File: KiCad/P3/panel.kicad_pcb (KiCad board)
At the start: 2 copper layers, 94 x 95.5 mm, 359 parts, among them J1 USB_C_Receptacle_USB2.0, J2 SM04B-SRSS-TB(LF)(SN), U1 USBLC6-2SC6

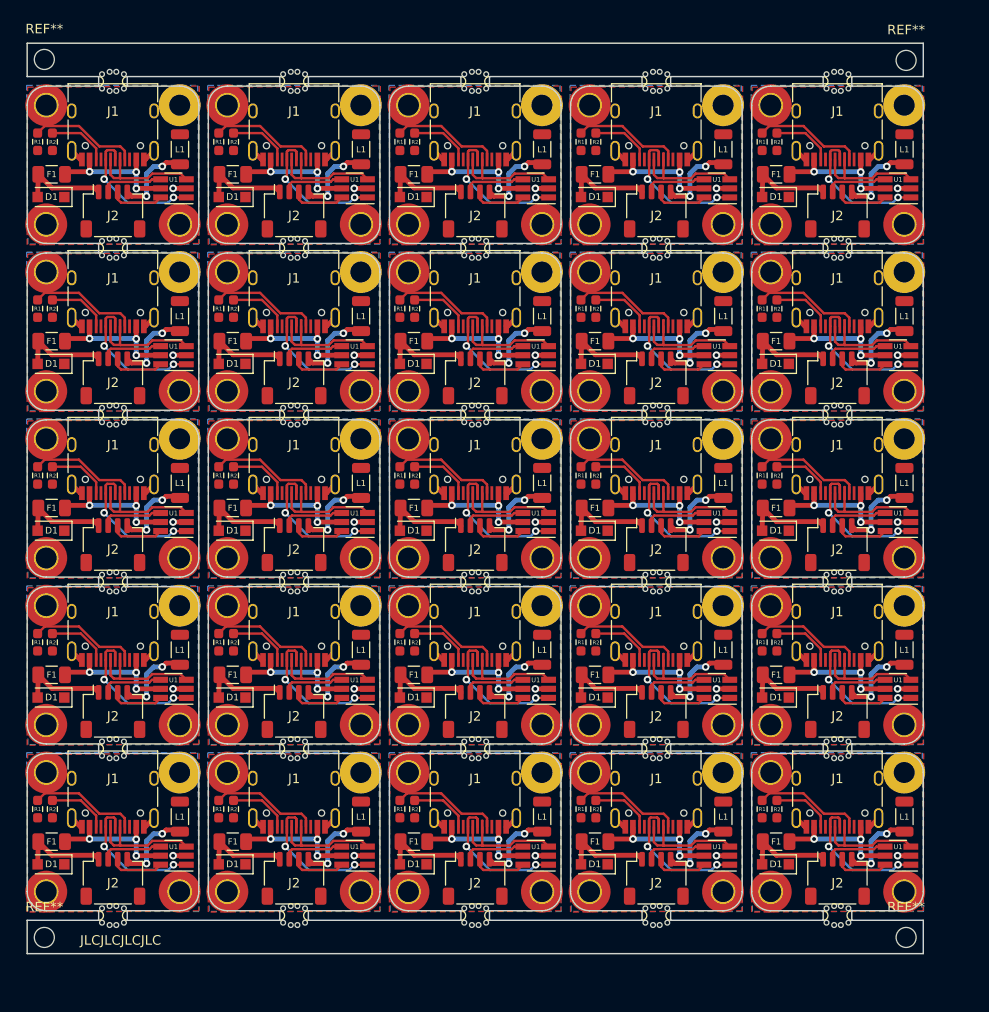
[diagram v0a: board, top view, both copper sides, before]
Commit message: Update P3 panel to improve mousebites and allow soldering before splitting
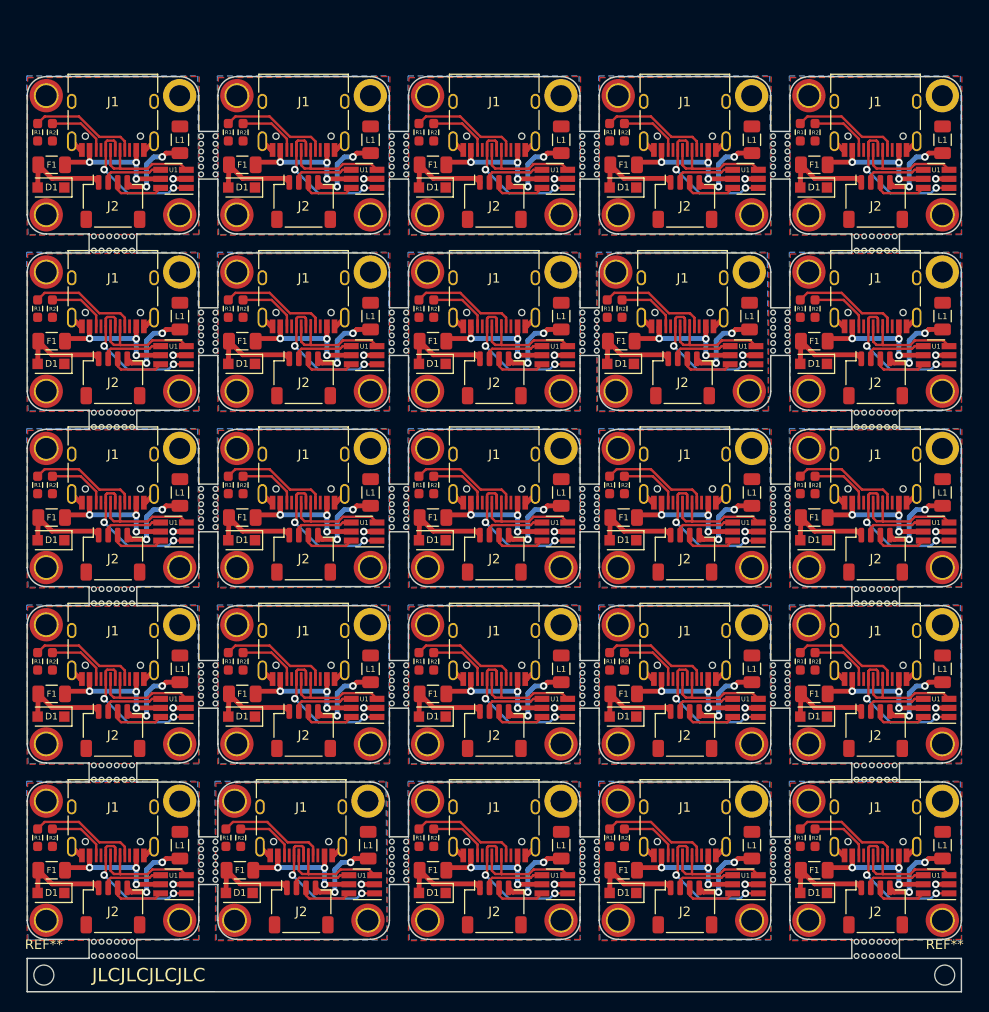
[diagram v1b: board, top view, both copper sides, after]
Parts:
- removed the D1 at (93.5, 101.0)
- removed the D1 at (17.5, 83.5)
- removed the D1 at (93.5, 66.0)
- removed the D1 at (74.5, 66.0)
- removed the D1 at (55.5, 66.0)
- removed the D1 at (36.5, 66.0)
- removed the D1 at (17.5, 66.0)
- removed the D1 at (93.5, 48.5)
- removed the D1 at (74.5, 48.5)
- removed the D1 at (55.5, 48.5)
- removed the D1 at (36.5, 48.5)
- removed the D1 at (74.5, 101.0)
- removed the D1 at (17.5, 48.5)
- removed the D1 at (93.5, 31.0)
- removed the D1 at (74.5, 31.0)
- removed the D1 at (55.5, 31.0)
- removed the D1 at (36.5, 31.0)
- removed the D1 at (17.5, 31.0)
- removed the D1 at (55.5, 101.0)
- removed the D1 at (36.5, 101.0)
- removed the D1 at (17.5, 101.0)
- removed the D1 at (93.5, 83.5)
- removed the D1 at (74.5, 83.5)
- removed the D1 at (55.5, 83.5)
- removed the D1 at (36.5, 83.5)
- removed the F1 at (74.6, 98.6)
- removed the F1 at (55.6, 81.1)
- removed the F1 at (74.6, 63.6)
- removed the F1 at (93.6, 63.6)
- removed the F1 at (17.6, 63.6)
- removed the F1 at (36.6, 63.6)
- removed the F1 at (55.6, 63.6)
- removed the F1 at (74.6, 46.1)
- removed the F1 at (93.6, 46.1)
- removed the F1 at (17.6, 46.1)
- removed the F1 at (36.6, 46.1)
- removed the F1 at (93.6, 98.6)
- removed the F1 at (55.6, 46.1)
- removed the F1 at (93.6, 28.6)
- removed the F1 at (74.6, 28.6)
- removed the F1 at (55.6, 28.6)
- removed the F1 at (36.6, 28.6)
- removed the F1 at (17.6, 28.6)
- removed the F1 at (17.6, 98.6)
- removed the F1 at (36.6, 98.6)
- removed the F1 at (55.6, 98.6)
- removed the F1 at (74.6, 81.1)
- removed the F1 at (93.6, 81.1)
- removed the F1 at (17.6, 81.1)
- removed the F1 at (36.6, 81.1)
- removed the G1 at (81.0, 99.8)
- removed the G1 at (62.0, 82.3)
- removed the G1 at (81.0, 64.8)
- removed the G1 at (100.0, 64.8)
- removed the G1 at (24.0, 64.8)
- removed the G1 at (43.0, 64.8)
- removed the G1 at (62.0, 64.8)
- removed the G1 at (81.0, 47.3)
- removed the G1 at (100.0, 47.3)
- removed the G1 at (24.0, 47.3)
- removed the G1 at (43.0, 47.3)
- removed the G1 at (100.0, 99.8)
- removed the G1 at (62.0, 47.3)
- removed the G1 at (100.0, 29.8)
- removed the G1 at (81.0, 29.8)
- removed the G1 at (62.0, 29.8)
- removed the G1 at (43.0, 29.8)
- removed the G1 at (24.0, 29.8)
- removed the G1 at (24.0, 99.8)
- removed the G1 at (43.0, 99.8)
- removed the G1 at (62.0, 99.8)
- removed the G1 at (81.0, 82.3)
- removed the G1 at (100.0, 82.3)
- removed the G1 at (24.0, 82.3)
- removed the G1 at (43.0, 82.3)
- removed the J1 at (100.0, 93.0)
- removed the J1 at (43.0, 75.5)
- removed the J1 at (100.0, 58.0)
- removed the J1 at (81.0, 58.0)
- removed the J1 at (62.0, 58.0)
- removed the J1 at (24.0, 58.0)
- removed the J1 at (43.0, 58.0)
- removed the J1 at (100.0, 40.5)
- removed the J1 at (81.0, 40.5)
- removed the J1 at (62.0, 40.5)
- removed the J1 at (24.0, 40.5)
- removed the J1 at (81.0, 93.0)
- removed the J1 at (43.0, 40.5)
- removed the J1 at (100.0, 23.0)
- removed the J1 at (81.0, 23.0)
- removed the J1 at (62.0, 23.0)
- removed the J1 at (43.0, 23.0)
- removed the J1 at (24.0, 23.0)
- removed the J1 at (62.0, 93.0)
- removed the J1 at (24.0, 93.0)
- removed the J1 at (43.0, 93.0)
- removed the J1 at (100.0, 75.5)
- removed the J1 at (81.0, 75.5)
- removed the J1 at (62.0, 75.5)
- removed the J1 at (24.0, 75.5)
- removed the J2 at (100.0, 102.4)
- removed the J2 at (62.0, 84.9)
- removed the J2 at (100.0, 67.4)
- removed the J2 at (81.0, 67.4)
- removed the J2 at (43.0, 67.4)
- removed the J2 at (24.0, 67.4)
- removed the J2 at (62.0, 67.4)
- removed the J2 at (100.0, 49.9)
- removed the J2 at (81.0, 49.9)
- removed the J2 at (43.0, 49.9)
- removed the J2 at (24.0, 49.9)
- removed the J2 at (81.0, 102.4)
- removed the J2 at (62.0, 49.9)
- removed the J2 at (100.0, 32.4)
- removed the J2 at (81.0, 32.4)
- removed the J2 at (62.0, 32.4)
- removed the J2 at (43.0, 32.4)
- removed the J2 at (24.0, 32.4)
- removed the J2 at (43.0, 102.4)
- removed the J2 at (24.0, 102.4)
- removed the J2 at (62.0, 102.4)
- removed the J2 at (100.0, 84.9)
- removed the J2 at (81.0, 84.9)
- removed the J2 at (43.0, 84.9)
- removed the J2 at (24.0, 84.9)
- removed the L1 at (107.0, 96.0)
- removed the L1 at (50.0, 78.5)
- removed the L1 at (107.0, 61.0)
- removed the L1 at (88.0, 61.0)
- removed the L1 at (31.0, 61.0)
- removed the L1 at (69.0, 61.0)
- removed the L1 at (50.0, 61.0)
- removed the L1 at (107.0, 43.5)
- removed the L1 at (88.0, 43.5)
- removed the L1 at (31.0, 43.5)
- removed the L1 at (69.0, 43.5)
- removed the L1 at (88.0, 96.0)
- removed the L1 at (50.0, 43.5)
- removed the L1 at (107.0, 26.0)
- removed the L1 at (88.0, 26.0)
- removed the L1 at (69.0, 26.0)
- removed the L1 at (50.0, 26.0)
- removed the L1 at (31.0, 26.0)
- removed the L1 at (31.0, 96.0)
- removed the L1 at (69.0, 96.0)
- removed the L1 at (50.0, 96.0)
- removed the L1 at (107.0, 78.5)
- removed the L1 at (88.0, 78.5)
- removed the L1 at (31.0, 78.5)
- removed the L1 at (69.0, 78.5)
- removed the MH1 at (93.0, 91.3)
- removed the MH1 at (55.0, 73.8)
- removed the MH1 at (93.0, 56.3)
- removed the MH1 at (74.0, 56.3)
- removed the MH1 at (36.0, 56.3)
- removed the MH1 at (17.0, 56.3)
- removed the MH1 at (55.0, 56.3)
- removed the MH1 at (93.0, 38.8)
- removed the MH1 at (74.0, 38.8)
- removed the MH1 at (36.0, 38.8)
- removed the MH1 at (17.0, 38.8)
- removed the MH1 at (74.0, 91.3)
- removed the MH1 at (55.0, 38.8)
- removed the MH1 at (93.0, 21.3)
- removed the MH1 at (74.0, 21.3)
- removed the MH1 at (55.0, 21.3)
- removed the MH1 at (36.0, 21.3)
- removed the MH1 at (17.0, 21.3)
- removed the MH1 at (36.0, 91.3)
- removed the MH1 at (17.0, 91.3)
- removed the MH1 at (55.0, 91.3)
- removed the MH1 at (93.0, 73.8)
- removed the MH1 at (74.0, 73.8)
- removed the MH1 at (36.0, 73.8)
- removed the MH1 at (17.0, 73.8)
- removed the MH2 at (107.0, 91.3)
- removed the MH2 at (69.0, 73.8)
- removed the MH2 at (107.0, 56.3)
- removed the MH2 at (88.0, 56.3)
- removed the MH2 at (50.0, 56.3)
- removed the MH2 at (31.0, 56.3)
- removed the MH2 at (69.0, 56.3)
- removed the MH2 at (107.0, 38.8)
- removed the MH2 at (88.0, 38.8)
- removed the MH2 at (50.0, 38.8)
- removed the MH2 at (31.0, 38.8)
- removed the MH2 at (88.0, 91.3)
- removed the MH2 at (69.0, 38.8)
- removed the MH2 at (107.0, 21.3)
- removed the MH2 at (88.0, 21.3)
- removed the MH2 at (69.0, 21.3)
- removed the MH2 at (50.0, 21.3)
- removed the MH2 at (31.0, 21.3)
- removed the MH2 at (50.0, 91.3)
- removed the MH2 at (31.0, 91.3)
- removed the MH2 at (69.0, 91.3)
- removed the MH2 at (107.0, 73.8)
- removed the MH2 at (88.0, 73.8)
- removed the MH2 at (50.0, 73.8)
- removed the MH2 at (31.0, 73.8)
- removed the MH3 at (93.0, 103.8)
- removed the MH3 at (55.0, 86.3)
- removed the MH3 at (93.0, 68.8)
- removed the MH3 at (74.0, 68.8)
- removed the MH3 at (36.0, 68.8)
- removed the MH3 at (17.0, 68.8)
- removed the MH3 at (55.0, 68.8)
- removed the MH3 at (93.0, 51.3)
- removed the MH3 at (74.0, 51.3)
- removed the MH3 at (36.0, 51.3)
- removed the MH3 at (17.0, 51.3)
- removed the MH3 at (74.0, 103.8)
- removed the MH3 at (55.0, 51.3)
- removed the MH3 at (93.0, 33.8)
- removed the MH3 at (74.0, 33.8)
- removed the MH3 at (55.0, 33.8)
- removed the MH3 at (36.0, 33.8)
- removed the MH3 at (17.0, 33.8)
- removed the MH3 at (36.0, 103.8)
- removed the MH3 at (17.0, 103.8)
- removed the MH3 at (55.0, 103.8)
- removed the MH3 at (93.0, 86.3)
- removed the MH3 at (74.0, 86.3)
- removed the MH3 at (36.0, 86.3)
- removed the MH3 at (17.0, 86.3)
- removed the MH4 at (107.0, 103.8)
- removed the MH4 at (69.0, 86.3)
- removed the MH4 at (107.0, 68.8)
- removed the MH4 at (88.0, 68.8)
- removed the MH4 at (50.0, 68.8)
- removed the MH4 at (31.0, 68.8)
- removed the MH4 at (69.0, 68.8)
- removed the MH4 at (107.0, 51.3)
- removed the MH4 at (88.0, 51.3)
- removed the MH4 at (50.0, 51.3)
- removed the MH4 at (31.0, 51.3)
- removed the MH4 at (88.0, 103.8)
- removed the MH4 at (69.0, 51.3)
- removed the MH4 at (107.0, 33.8)
- removed the MH4 at (88.0, 33.8)
- removed the MH4 at (69.0, 33.8)
- removed the MH4 at (50.0, 33.8)
- removed the MH4 at (31.0, 33.8)
- removed the MH4 at (50.0, 103.8)
- removed the MH4 at (31.0, 103.8)
- removed the MH4 at (69.0, 103.8)
- removed the MH4 at (107.0, 86.3)
- removed the MH4 at (88.0, 86.3)
- removed the MH4 at (50.0, 86.3)
- removed the MH4 at (31.0, 86.3)
- removed the R1 at (92.1, 95.2)
- removed the R1 at (35.1, 77.7)
- removed the R1 at (92.1, 60.2)
- removed the R1 at (73.1, 60.2)
- removed the R1 at (54.1, 60.2)
- removed the R1 at (16.1, 60.2)
- removed the R1 at (35.1, 60.2)
- removed the R1 at (92.1, 42.7)
- removed the R1 at (73.1, 42.7)
- removed the R1 at (54.1, 42.7)
- removed the R1 at (16.1, 42.7)
- removed the R1 at (73.1, 95.2)
- removed the R1 at (35.1, 42.7)
- removed the R1 at (92.1, 25.2)
- removed the R1 at (73.1, 25.2)
- removed the R1 at (54.1, 25.2)
- removed the R1 at (35.1, 25.2)
- removed the R1 at (16.1, 25.2)
- removed the R1 at (54.1, 95.2)
- removed the R1 at (16.1, 95.2)
- removed the R1 at (35.1, 95.2)
- removed the R1 at (92.1, 77.7)
- removed the R1 at (73.1, 77.7)
- removed the R1 at (54.1, 77.7)
- removed the R1 at (16.1, 77.7)
- removed the R2 at (93.6, 95.2)
- removed the R2 at (17.6, 77.7)
- removed the R2 at (93.6, 60.2)
- removed the R2 at (36.6, 60.2)
- removed the R2 at (74.6, 60.2)
- removed the R2 at (55.6, 60.2)
- removed the R2 at (17.6, 60.2)
- removed the R2 at (93.6, 42.7)
- removed the R2 at (36.6, 42.7)
- removed the R2 at (74.6, 42.7)
- removed the R2 at (55.6, 42.7)
- removed the R2 at (36.6, 95.2)
- removed the R2 at (17.6, 42.7)
- removed the R2 at (93.7, 25.2)
- removed the R2 at (74.7, 25.2)
- removed the R2 at (55.7, 25.2)
- removed the R2 at (36.7, 25.2)
- removed the R2 at (17.7, 25.2)
- removed the R2 at (74.6, 95.2)
- removed the R2 at (55.6, 95.2)
- removed the R2 at (17.6, 95.2)
- removed the R2 at (93.6, 77.7)
- removed the R2 at (36.6, 77.7)
- removed the R2 at (74.6, 77.7)
- removed the R2 at (55.6, 77.7)
- removed the REF** at (107.2, 16.6)
- removed the REF** at (16.8, 16.5)
- removed the REF** at (107.2, 108.6)
- removed the REF** at (16.8, 108.6)
- removed the U1 at (106.3, 100.1)
- removed the U1 at (49.3, 82.6)
- removed the U1 at (106.3, 65.1)
- removed the U1 at (87.3, 65.1)
- removed the U1 at (68.3, 65.1)
- removed the U1 at (30.3, 65.1)
- removed the U1 at (49.3, 65.1)
- removed the U1 at (106.3, 47.6)
- removed the U1 at (87.3, 47.6)
- removed the U1 at (68.3, 47.6)
- removed the U1 at (30.3, 47.6)
- removed the U1 at (87.3, 100.1)
- removed the U1 at (49.3, 47.6)
- removed the U1 at (106.4, 30.1)
- removed the U1 at (87.4, 30.1)
- removed the U1 at (68.4, 30.1)
- removed the U1 at (49.4, 30.1)
- removed the U1 at (30.4, 30.1)
- removed the U1 at (68.3, 100.1)
- removed the U1 at (30.3, 100.1)
- removed the U1 at (49.3, 100.1)
- removed the U1 at (106.3, 82.6)
- removed the U1 at (87.3, 82.6)
- removed the U1 at (68.3, 82.6)
- removed the U1 at (30.3, 82.6)
- removed the mouse-bite-1mm-slot at (24.0, 106.3)
- removed the mouse-bite-1mm-slot at (24.0, 88.8)
- removed the mouse-bite-1mm-slot at (24.0, 71.3)
- removed the mouse-bite-1mm-slot at (43.0, 71.3)
- removed the mouse-bite-1mm-slot at (62.0, 71.3)
- removed the mouse-bite-1mm-slot at (81.0, 71.3)
- removed the mouse-bite-1mm-slot at (100.0, 71.3)
- removed the mouse-bite-1mm-slot at (100.0, 53.8)
- removed the mouse-bite-1mm-slot at (81.0, 53.8)
- removed the mouse-bite-1mm-slot at (62.0, 53.8)
- removed the mouse-bite-1mm-slot at (43.0, 53.8)
- removed the mouse-bite-1mm-slot at (43.0, 106.3)
- removed the mouse-bite-1mm-slot at (24.0, 53.8)
- removed the mouse-bite-1mm-slot at (24.0, 36.3)
- removed the mouse-bite-1mm-slot at (43.0, 36.3)
- removed the mouse-bite-1mm-slot at (62.0, 36.3)
- removed the mouse-bite-1mm-slot at (81.0, 36.3)
- removed the mouse-bite-1mm-slot at (100.0, 36.3)
- removed the mouse-bite-1mm-slot at (100.0, 18.8)
- removed the mouse-bite-1mm-slot at (81.0, 18.8)
- removed the mouse-bite-1mm-slot at (62.0, 18.8)
- removed the mouse-bite-1mm-slot at (43.0, 18.8)
- removed the mouse-bite-1mm-slot at (62.0, 106.3)
- removed the mouse-bite-1mm-slot at (24.0, 18.8)
- removed the mouse-bite-1mm-slot at (81.0, 106.3)
- removed the mouse-bite-1mm-slot at (100.0, 106.3)
- removed the mouse-bite-1mm-slot at (100.0, 88.8)
- removed the mouse-bite-1mm-slot at (81.0, 88.8)
- removed the mouse-bite-1mm-slot at (62.0, 88.8)
- removed the mouse-bite-1mm-slot at (43.0, 88.8)
- added D1: SMF9.0CA, Diode_SMD:D_SOD-123F, F.Cu at (17.5, 104.0)
- added D1: SMF9.0CA, Diode_SMD:D_SOD-123F, F.Cu at (17.5, 85.5)
- added D1: SMF9.0CA, Diode_SMD:D_SOD-123F, F.Cu at (17.5, 67.0)
- added D1: SMF9.0CA, Diode_SMD:D_SOD-123F, F.Cu at (37.5, 67.0)
- added D1: SMF9.0CA, Diode_SMD:D_SOD-123F, F.Cu at (57.5, 67.0)
- added D1: SMF9.0CA, Diode_SMD:D_SOD-123F, F.Cu at (77.5, 67.0)
- added D1: SMF9.0CA, Diode_SMD:D_SOD-123F, F.Cu at (97.5, 67.0)
- added D1: SMF9.0CA, Diode_SMD:D_SOD-123F, F.Cu at (97.5, 48.5)
- added D1: SMF9.0CA, Diode_SMD:D_SOD-123F, F.Cu at (77.3, 48.5)
- added D1: SMF9.0CA, Diode_SMD:D_SOD-123F, F.Cu at (57.5, 48.5)
- added D1: SMF9.0CA, Diode_SMD:D_SOD-123F, F.Cu at (37.5, 48.5)
- added D1: SMF9.0CA, Diode_SMD:D_SOD-123F, F.Cu at (37.3, 104.0)
- added D1: SMF9.0CA, Diode_SMD:D_SOD-123F, F.Cu at (17.5, 48.5)
- added D1: SMF9.0CA, Diode_SMD:D_SOD-123F, F.Cu at (97.5, 30.0)
- added D1: SMF9.0CA, Diode_SMD:D_SOD-123F, F.Cu at (77.5, 30.0)
- added D1: SMF9.0CA, Diode_SMD:D_SOD-123F, F.Cu at (57.5, 30.0)
- added D1: SMF9.0CA, Diode_SMD:D_SOD-123F, F.Cu at (37.5, 30.0)
- added D1: SMF9.0CA, Diode_SMD:D_SOD-123F, F.Cu at (17.5, 30.0)
- added D1: SMF9.0CA, Diode_SMD:D_SOD-123F, F.Cu at (57.5, 104.0)
- added D1: SMF9.0CA, Diode_SMD:D_SOD-123F, F.Cu at (77.5, 104.0)
- added D1: SMF9.0CA, Diode_SMD:D_SOD-123F, F.Cu at (97.5, 104.0)
- added D1: SMF9.0CA, Diode_SMD:D_SOD-123F, F.Cu at (97.5, 85.5)
- added D1: SMF9.0CA, Diode_SMD:D_SOD-123F, F.Cu at (77.5, 85.5)
- added D1: SMF9.0CA, Diode_SMD:D_SOD-123F, F.Cu at (57.5, 85.5)
- added D1: SMF9.0CA, Diode_SMD:D_SOD-123F, F.Cu at (37.5, 85.5)
- added F1: ASMD1206-150, Fuse:Fuse_1206_3216Metric, F.Cu at (17.6, 101.6)
- added F1: ASMD1206-150, Fuse:Fuse_1206_3216Metric, F.Cu at (17.6, 83.1)
- added F1: ASMD1206-150, Fuse:Fuse_1206_3216Metric, F.Cu at (17.6, 64.6)
- added F1: ASMD1206-150, Fuse:Fuse_1206_3216Metric, F.Cu at (37.6, 64.6)
- added F1: ASMD1206-150, Fuse:Fuse_1206_3216Metric, F.Cu at (57.6, 64.6)
- added F1: ASMD1206-150, Fuse:Fuse_1206_3216Metric, F.Cu at (77.6, 64.6)
- added F1: ASMD1206-150, Fuse:Fuse_1206_3216Metric, F.Cu at (97.6, 64.6)
- added F1: ASMD1206-150, Fuse:Fuse_1206_3216Metric, F.Cu at (97.6, 46.1)
- added F1: ASMD1206-150, Fuse:Fuse_1206_3216Metric, F.Cu at (77.3, 46.1)
- added F1: ASMD1206-150, Fuse:Fuse_1206_3216Metric, F.Cu at (57.6, 46.1)
- added F1: ASMD1206-150, Fuse:Fuse_1206_3216Metric, F.Cu at (37.6, 46.1)
- added F1: ASMD1206-150, Fuse:Fuse_1206_3216Metric, F.Cu at (37.3, 101.6)
- added F1: ASMD1206-150, Fuse:Fuse_1206_3216Metric, F.Cu at (17.6, 46.1)
- added F1: ASMD1206-150, Fuse:Fuse_1206_3216Metric, F.Cu at (97.6, 27.6)
- added F1: ASMD1206-150, Fuse:Fuse_1206_3216Metric, F.Cu at (77.6, 27.6)
- added F1: ASMD1206-150, Fuse:Fuse_1206_3216Metric, F.Cu at (57.6, 27.6)
- added F1: ASMD1206-150, Fuse:Fuse_1206_3216Metric, F.Cu at (37.6, 27.6)
- added F1: ASMD1206-150, Fuse:Fuse_1206_3216Metric, F.Cu at (17.6, 27.6)
- added F1: ASMD1206-150, Fuse:Fuse_1206_3216Metric, F.Cu at (57.6, 101.6)
- added F1: ASMD1206-150, Fuse:Fuse_1206_3216Metric, F.Cu at (77.6, 101.6)
- added F1: ASMD1206-150, Fuse:Fuse_1206_3216Metric, F.Cu at (97.6, 101.6)
- added F1: ASMD1206-150, Fuse:Fuse_1206_3216Metric, F.Cu at (97.6, 83.1)
- added F1: ASMD1206-150, Fuse:Fuse_1206_3216Metric, F.Cu at (77.6, 83.1)
- added F1: ASMD1206-150, Fuse:Fuse_1206_3216Metric, F.Cu at (57.6, 83.1)
- added F1: ASMD1206-150, Fuse:Fuse_1206_3216Metric, F.Cu at (37.6, 83.1)
- added G1: Unified-Daughterboard-Logo, Unified-Daughterboard-Logo:Unified-Daughterboard-Logo.pretty, B.Cu at (24.0, 102.8)
- added G1: Unified-Daughterboard-Logo, Unified-Daughterboard-Logo:Unified-Daughterboard-Logo.pretty, B.Cu at (24.0, 84.3)
- added G1: Unified-Daughterboard-Logo, Unified-Daughterboard-Logo:Unified-Daughterboard-Logo.pretty, B.Cu at (24.0, 65.8)
- added G1: Unified-Daughterboard-Logo, Unified-Daughterboard-Logo:Unified-Daughterboard-Logo.pretty, B.Cu at (44.0, 65.8)
- added G1: Unified-Daughterboard-Logo, Unified-Daughterboard-Logo:Unified-Daughterboard-Logo.pretty, B.Cu at (64.0, 65.8)
- added G1: Unified-Daughterboard-Logo, Unified-Daughterboard-Logo:Unified-Daughterboard-Logo.pretty, B.Cu at (84.0, 65.8)
- added G1: Unified-Daughterboard-Logo, Unified-Daughterboard-Logo:Unified-Daughterboard-Logo.pretty, B.Cu at (104.0, 65.8)
- added G1: Unified-Daughterboard-Logo, Unified-Daughterboard-Logo:Unified-Daughterboard-Logo.pretty, B.Cu at (104.0, 47.3)
- added G1: Unified-Daughterboard-Logo, Unified-Daughterboard-Logo:Unified-Daughterboard-Logo.pretty, B.Cu at (83.8, 47.3)
- added G1: Unified-Daughterboard-Logo, Unified-Daughterboard-Logo:Unified-Daughterboard-Logo.pretty, B.Cu at (64.0, 47.3)
- added G1: Unified-Daughterboard-Logo, Unified-Daughterboard-Logo:Unified-Daughterboard-Logo.pretty, B.Cu at (44.0, 47.3)
- added G1: Unified-Daughterboard-Logo, Unified-Daughterboard-Logo:Unified-Daughterboard-Logo.pretty, B.Cu at (43.8, 102.8)
- added G1: Unified-Daughterboard-Logo, Unified-Daughterboard-Logo:Unified-Daughterboard-Logo.pretty, B.Cu at (24.0, 47.3)
- added G1: Unified-Daughterboard-Logo, Unified-Daughterboard-Logo:Unified-Daughterboard-Logo.pretty, B.Cu at (104.0, 28.8)
- added G1: Unified-Daughterboard-Logo, Unified-Daughterboard-Logo:Unified-Daughterboard-Logo.pretty, B.Cu at (84.0, 28.8)
- added G1: Unified-Daughterboard-Logo, Unified-Daughterboard-Logo:Unified-Daughterboard-Logo.pretty, B.Cu at (64.0, 28.8)
- added G1: Unified-Daughterboard-Logo, Unified-Daughterboard-Logo:Unified-Daughterboard-Logo.pretty, B.Cu at (44.0, 28.8)
- added G1: Unified-Daughterboard-Logo, Unified-Daughterboard-Logo:Unified-Daughterboard-Logo.pretty, B.Cu at (24.0, 28.8)
- added G1: Unified-Daughterboard-Logo, Unified-Daughterboard-Logo:Unified-Daughterboard-Logo.pretty, B.Cu at (64.0, 102.8)
- added G1: Unified-Daughterboard-Logo, Unified-Daughterboard-Logo:Unified-Daughterboard-Logo.pretty, B.Cu at (84.0, 102.8)
- added G1: Unified-Daughterboard-Logo, Unified-Daughterboard-Logo:Unified-Daughterboard-Logo.pretty, B.Cu at (104.0, 102.8)
- added G1: Unified-Daughterboard-Logo, Unified-Daughterboard-Logo:Unified-Daughterboard-Logo.pretty, B.Cu at (104.0, 84.3)
- added G1: Unified-Daughterboard-Logo, Unified-Daughterboard-Logo:Unified-Daughterboard-Logo.pretty, B.Cu at (84.0, 84.3)
- added G1: Unified-Daughterboard-Logo, Unified-Daughterboard-Logo:Unified-Daughterboard-Logo.pretty, B.Cu at (64.0, 84.3)
- added G1: Unified-Daughterboard-Logo, Unified-Daughterboard-Logo:Unified-Daughterboard-Logo.pretty, B.Cu at (44.0, 84.3)
- added J1: USB_C_Receptacle_USB2.0, Connector_USB:USB_C_Receptacle_HRO_TYPE-C-31-M-12, F.Cu at (24.0, 96.0)
- added J1: USB_C_Receptacle_USB2.0, Connector_USB:USB_C_Receptacle_HRO_TYPE-C-31-M-12, F.Cu at (24.0, 77.5)
- added J1: USB_C_Receptacle_USB2.0, Connector_USB:USB_C_Receptacle_HRO_TYPE-C-31-M-12, F.Cu at (24.0, 59.0)
- added J1: USB_C_Receptacle_USB2.0, Connector_USB:USB_C_Receptacle_HRO_TYPE-C-31-M-12, F.Cu at (44.0, 59.0)
- added J1: USB_C_Receptacle_USB2.0, Connector_USB:USB_C_Receptacle_HRO_TYPE-C-31-M-12, F.Cu at (64.0, 59.0)
- added J1: USB_C_Receptacle_USB2.0, Connector_USB:USB_C_Receptacle_HRO_TYPE-C-31-M-12, F.Cu at (84.0, 59.0)
- added J1: USB_C_Receptacle_USB2.0, Connector_USB:USB_C_Receptacle_HRO_TYPE-C-31-M-12, F.Cu at (104.0, 59.0)
- added J1: USB_C_Receptacle_USB2.0, Connector_USB:USB_C_Receptacle_HRO_TYPE-C-31-M-12, F.Cu at (104.0, 40.5)
- added J1: USB_C_Receptacle_USB2.0, Connector_USB:USB_C_Receptacle_HRO_TYPE-C-31-M-12, F.Cu at (83.7, 40.5)
- added J1: USB_C_Receptacle_USB2.0, Connector_USB:USB_C_Receptacle_HRO_TYPE-C-31-M-12, F.Cu at (64.0, 40.5)
- added J1: USB_C_Receptacle_USB2.0, Connector_USB:USB_C_Receptacle_HRO_TYPE-C-31-M-12, F.Cu at (44.0, 40.5)
- added J1: USB_C_Receptacle_USB2.0, Connector_USB:USB_C_Receptacle_HRO_TYPE-C-31-M-12, F.Cu at (43.7, 96.0)
- added J1: USB_C_Receptacle_USB2.0, Connector_USB:USB_C_Receptacle_HRO_TYPE-C-31-M-12, F.Cu at (24.0, 40.5)
- added J1: USB_C_Receptacle_USB2.0, Connector_USB:USB_C_Receptacle_HRO_TYPE-C-31-M-12, F.Cu at (104.0, 22.0)
- added J1: USB_C_Receptacle_USB2.0, Connector_USB:USB_C_Receptacle_HRO_TYPE-C-31-M-12, F.Cu at (84.0, 22.0)
- added J1: USB_C_Receptacle_USB2.0, Connector_USB:USB_C_Receptacle_HRO_TYPE-C-31-M-12, F.Cu at (64.0, 22.0)
- added J1: USB_C_Receptacle_USB2.0, Connector_USB:USB_C_Receptacle_HRO_TYPE-C-31-M-12, F.Cu at (44.0, 22.0)
- added J1: USB_C_Receptacle_USB2.0, Connector_USB:USB_C_Receptacle_HRO_TYPE-C-31-M-12, F.Cu at (24.0, 22.0)
- added J1: USB_C_Receptacle_USB2.0, Connector_USB:USB_C_Receptacle_HRO_TYPE-C-31-M-12, F.Cu at (64.0, 96.0)
- added J1: USB_C_Receptacle_USB2.0, Connector_USB:USB_C_Receptacle_HRO_TYPE-C-31-M-12, F.Cu at (84.0, 96.0)
- added J1: USB_C_Receptacle_USB2.0, Connector_USB:USB_C_Receptacle_HRO_TYPE-C-31-M-12, F.Cu at (104.0, 96.0)
- added J1: USB_C_Receptacle_USB2.0, Connector_USB:USB_C_Receptacle_HRO_TYPE-C-31-M-12, F.Cu at (104.0, 77.5)
- added J1: USB_C_Receptacle_USB2.0, Connector_USB:USB_C_Receptacle_HRO_TYPE-C-31-M-12, F.Cu at (84.0, 77.5)
- added J1: USB_C_Receptacle_USB2.0, Connector_USB:USB_C_Receptacle_HRO_TYPE-C-31-M-12, F.Cu at (64.0, 77.5)
- added J1: USB_C_Receptacle_USB2.0, Connector_USB:USB_C_Receptacle_HRO_TYPE-C-31-M-12, F.Cu at (44.0, 77.5)
- added J2: SM04B-SRSS-TB(LF)(SN), Connector_JST:JST_SH_SM04B-SRSS-TB_1x04-1MP_P1.00mm_Horizontal, F.Cu at (24.0, 105.4)
- added J2: SM04B-SRSS-TB(LF)(SN), Connector_JST:JST_SH_SM04B-SRSS-TB_1x04-1MP_P1.00mm_Horizontal, F.Cu at (24.0, 86.9)
- added J2: SM04B-SRSS-TB(LF)(SN), Connector_JST:JST_SH_SM04B-SRSS-TB_1x04-1MP_P1.00mm_Horizontal, F.Cu at (24.0, 68.4)
- added J2: SM04B-SRSS-TB(LF)(SN), Connector_JST:JST_SH_SM04B-SRSS-TB_1x04-1MP_P1.00mm_Horizontal, F.Cu at (44.0, 68.4)
- added J2: SM04B-SRSS-TB(LF)(SN), Connector_JST:JST_SH_SM04B-SRSS-TB_1x04-1MP_P1.00mm_Horizontal, F.Cu at (64.0, 68.4)
- added J2: SM04B-SRSS-TB(LF)(SN), Connector_JST:JST_SH_SM04B-SRSS-TB_1x04-1MP_P1.00mm_Horizontal, F.Cu at (84.0, 68.4)
- added J2: SM04B-SRSS-TB(LF)(SN), Connector_JST:JST_SH_SM04B-SRSS-TB_1x04-1MP_P1.00mm_Horizontal, F.Cu at (104.0, 68.4)
- added J2: SM04B-SRSS-TB(LF)(SN), Connector_JST:JST_SH_SM04B-SRSS-TB_1x04-1MP_P1.00mm_Horizontal, F.Cu at (104.0, 49.9)
- added J2: SM04B-SRSS-TB(LF)(SN), Connector_JST:JST_SH_SM04B-SRSS-TB_1x04-1MP_P1.00mm_Horizontal, F.Cu at (83.8, 49.9)
- added J2: SM04B-SRSS-TB(LF)(SN), Connector_JST:JST_SH_SM04B-SRSS-TB_1x04-1MP_P1.00mm_Horizontal, F.Cu at (64.0, 49.9)
- added J2: SM04B-SRSS-TB(LF)(SN), Connector_JST:JST_SH_SM04B-SRSS-TB_1x04-1MP_P1.00mm_Horizontal, F.Cu at (44.0, 49.9)
- added J2: SM04B-SRSS-TB(LF)(SN), Connector_JST:JST_SH_SM04B-SRSS-TB_1x04-1MP_P1.00mm_Horizontal, F.Cu at (43.8, 105.4)
- added J2: SM04B-SRSS-TB(LF)(SN), Connector_JST:JST_SH_SM04B-SRSS-TB_1x04-1MP_P1.00mm_Horizontal, F.Cu at (24.0, 49.9)
- added J2: SM04B-SRSS-TB(LF)(SN), Connector_JST:JST_SH_SM04B-SRSS-TB_1x04-1MP_P1.00mm_Horizontal, F.Cu at (104.0, 31.4)
- added J2: SM04B-SRSS-TB(LF)(SN), Connector_JST:JST_SH_SM04B-SRSS-TB_1x04-1MP_P1.00mm_Horizontal, F.Cu at (84.0, 31.4)
- added J2: SM04B-SRSS-TB(LF)(SN), Connector_JST:JST_SH_SM04B-SRSS-TB_1x04-1MP_P1.00mm_Horizontal, F.Cu at (64.0, 31.4)
- added J2: SM04B-SRSS-TB(LF)(SN), Connector_JST:JST_SH_SM04B-SRSS-TB_1x04-1MP_P1.00mm_Horizontal, F.Cu at (44.0, 31.4)
- added J2: SM04B-SRSS-TB(LF)(SN), Connector_JST:JST_SH_SM04B-SRSS-TB_1x04-1MP_P1.00mm_Horizontal, F.Cu at (24.0, 31.4)
- added J2: SM04B-SRSS-TB(LF)(SN), Connector_JST:JST_SH_SM04B-SRSS-TB_1x04-1MP_P1.00mm_Horizontal, F.Cu at (64.0, 105.4)
- added J2: SM04B-SRSS-TB(LF)(SN), Connector_JST:JST_SH_SM04B-SRSS-TB_1x04-1MP_P1.00mm_Horizontal, F.Cu at (84.0, 105.4)
- added J2: SM04B-SRSS-TB(LF)(SN), Connector_JST:JST_SH_SM04B-SRSS-TB_1x04-1MP_P1.00mm_Horizontal, F.Cu at (104.0, 105.4)
- added J2: SM04B-SRSS-TB(LF)(SN), Connector_JST:JST_SH_SM04B-SRSS-TB_1x04-1MP_P1.00mm_Horizontal, F.Cu at (104.0, 86.9)
- added J2: SM04B-SRSS-TB(LF)(SN), Connector_JST:JST_SH_SM04B-SRSS-TB_1x04-1MP_P1.00mm_Horizontal, F.Cu at (84.0, 86.9)
- added J2: SM04B-SRSS-TB(LF)(SN), Connector_JST:JST_SH_SM04B-SRSS-TB_1x04-1MP_P1.00mm_Horizontal, F.Cu at (64.0, 86.9)
- added J2: SM04B-SRSS-TB(LF)(SN), Connector_JST:JST_SH_SM04B-SRSS-TB_1x04-1MP_P1.00mm_Horizontal, F.Cu at (44.0, 86.9)
- added L1: 60R@100MHz, Inductor_SMD:L_1206_3216Metric, F.Cu at (31.0, 99.0)
- added L1: 60R@100MHz, Inductor_SMD:L_1206_3216Metric, F.Cu at (31.0, 80.5)
- added L1: 60R@100MHz, Inductor_SMD:L_1206_3216Metric, F.Cu at (31.0, 62.0)
- added L1: 60R@100MHz, Inductor_SMD:L_1206_3216Metric, F.Cu at (51.0, 62.0)
- added L1: 60R@100MHz, Inductor_SMD:L_1206_3216Metric, F.Cu at (71.0, 62.0)
- added L1: 60R@100MHz, Inductor_SMD:L_1206_3216Metric, F.Cu at (91.0, 62.0)
- added L1: 60R@100MHz, Inductor_SMD:L_1206_3216Metric, F.Cu at (111.0, 62.0)
- added L1: 60R@100MHz, Inductor_SMD:L_1206_3216Metric, F.Cu at (111.0, 43.5)
- added L1: 60R@100MHz, Inductor_SMD:L_1206_3216Metric, F.Cu at (90.8, 43.5)
- added L1: 60R@100MHz, Inductor_SMD:L_1206_3216Metric, F.Cu at (71.0, 43.5)
- added L1: 60R@100MHz, Inductor_SMD:L_1206_3216Metric, F.Cu at (51.0, 43.5)
- added L1: 60R@100MHz, Inductor_SMD:L_1206_3216Metric, F.Cu at (50.8, 99.0)
- added L1: 60R@100MHz, Inductor_SMD:L_1206_3216Metric, F.Cu at (31.0, 43.5)
- added L1: 60R@100MHz, Inductor_SMD:L_1206_3216Metric, F.Cu at (111.0, 25.0)
- added L1: 60R@100MHz, Inductor_SMD:L_1206_3216Metric, F.Cu at (91.0, 25.0)
- added L1: 60R@100MHz, Inductor_SMD:L_1206_3216Metric, F.Cu at (71.0, 25.0)
- added L1: 60R@100MHz, Inductor_SMD:L_1206_3216Metric, F.Cu at (51.0, 25.0)
- added L1: 60R@100MHz, Inductor_SMD:L_1206_3216Metric, F.Cu at (31.0, 25.0)
- added L1: 60R@100MHz, Inductor_SMD:L_1206_3216Metric, F.Cu at (71.0, 99.0)
- added L1: 60R@100MHz, Inductor_SMD:L_1206_3216Metric, F.Cu at (91.0, 99.0)
- added L1: 60R@100MHz, Inductor_SMD:L_1206_3216Metric, F.Cu at (111.0, 99.0)
- added L1: 60R@100MHz, Inductor_SMD:L_1206_3216Metric, F.Cu at (111.0, 80.5)
- added L1: 60R@100MHz, Inductor_SMD:L_1206_3216Metric, F.Cu at (91.0, 80.5)
- added L1: 60R@100MHz, Inductor_SMD:L_1206_3216Metric, F.Cu at (71.0, 80.5)
- added L1: 60R@100MHz, Inductor_SMD:L_1206_3216Metric, F.Cu at (51.0, 80.5)
- added MH1: Mount-M2, MountingHole:MountingHole_2.2mm_M2_Pad_TopOnly, F.Cu at (17.0, 94.3)
- added MH1: Mount-M2, MountingHole:MountingHole_2.2mm_M2_Pad_TopOnly, F.Cu at (17.0, 75.8)
- added MH1: Mount-M2, MountingHole:MountingHole_2.2mm_M2_Pad_TopOnly, F.Cu at (17.0, 57.3)
- added MH1: Mount-M2, MountingHole:MountingHole_2.2mm_M2_Pad_TopOnly, F.Cu at (37.0, 57.3)
- added MH1: Mount-M2, MountingHole:MountingHole_2.2mm_M2_Pad_TopOnly, F.Cu at (57.0, 57.3)
- added MH1: Mount-M2, MountingHole:MountingHole_2.2mm_M2_Pad_TopOnly, F.Cu at (77.0, 57.3)
- added MH1: Mount-M2, MountingHole:MountingHole_2.2mm_M2_Pad_TopOnly, F.Cu at (97.0, 57.3)
- added MH1: Mount-M2, MountingHole:MountingHole_2.2mm_M2_Pad_TopOnly, F.Cu at (97.0, 38.8)
- added MH1: Mount-M2, MountingHole:MountingHole_2.2mm_M2_Pad_TopOnly, F.Cu at (76.8, 38.8)
- added MH1: Mount-M2, MountingHole:MountingHole_2.2mm_M2_Pad_TopOnly, F.Cu at (57.0, 38.8)
- added MH1: Mount-M2, MountingHole:MountingHole_2.2mm_M2_Pad_TopOnly, F.Cu at (37.0, 38.8)
- added MH1: Mount-M2, MountingHole:MountingHole_2.2mm_M2_Pad_TopOnly, F.Cu at (36.8, 94.3)
- added MH1: Mount-M2, MountingHole:MountingHole_2.2mm_M2_Pad_TopOnly, F.Cu at (17.0, 38.8)
- added MH1: Mount-M2, MountingHole:MountingHole_2.2mm_M2_Pad_TopOnly, F.Cu at (97.0, 20.3)
- added MH1: Mount-M2, MountingHole:MountingHole_2.2mm_M2_Pad_TopOnly, F.Cu at (77.0, 20.3)
- added MH1: Mount-M2, MountingHole:MountingHole_2.2mm_M2_Pad_TopOnly, F.Cu at (57.0, 20.3)
- added MH1: Mount-M2, MountingHole:MountingHole_2.2mm_M2_Pad_TopOnly, F.Cu at (37.0, 20.3)
- added MH1: Mount-M2, MountingHole:MountingHole_2.2mm_M2_Pad_TopOnly, F.Cu at (17.0, 20.3)
- added MH1: Mount-M2, MountingHole:MountingHole_2.2mm_M2_Pad_TopOnly, F.Cu at (57.0, 94.3)
- added MH1: Mount-M2, MountingHole:MountingHole_2.2mm_M2_Pad_TopOnly, F.Cu at (77.0, 94.3)
- added MH1: Mount-M2, MountingHole:MountingHole_2.2mm_M2_Pad_TopOnly, F.Cu at (97.0, 94.3)
- added MH1: Mount-M2, MountingHole:MountingHole_2.2mm_M2_Pad_TopOnly, F.Cu at (97.0, 75.8)
- added MH1: Mount-M2, MountingHole:MountingHole_2.2mm_M2_Pad_TopOnly, F.Cu at (77.0, 75.8)
- added MH1: Mount-M2, MountingHole:MountingHole_2.2mm_M2_Pad_TopOnly, F.Cu at (57.0, 75.8)
- added MH1: Mount-M2, MountingHole:MountingHole_2.2mm_M2_Pad_TopOnly, F.Cu at (37.0, 75.8)
- added MH2: Mount-M2, MountingHole:MountingHole_2.2mm_M2_Pad, F.Cu at (31.0, 94.3)
- added MH2: Mount-M2, MountingHole:MountingHole_2.2mm_M2_Pad, F.Cu at (31.0, 75.8)
- added MH2: Mount-M2, MountingHole:MountingHole_2.2mm_M2_Pad, F.Cu at (31.0, 57.3)
- added MH2: Mount-M2, MountingHole:MountingHole_2.2mm_M2_Pad, F.Cu at (51.0, 57.3)
- added MH2: Mount-M2, MountingHole:MountingHole_2.2mm_M2_Pad, F.Cu at (71.0, 57.3)
- added MH2: Mount-M2, MountingHole:MountingHole_2.2mm_M2_Pad, F.Cu at (91.0, 57.3)
- added MH2: Mount-M2, MountingHole:MountingHole_2.2mm_M2_Pad, F.Cu at (111.0, 57.3)
- added MH2: Mount-M2, MountingHole:MountingHole_2.2mm_M2_Pad, F.Cu at (111.0, 38.8)
- added MH2: Mount-M2, MountingHole:MountingHole_2.2mm_M2_Pad, F.Cu at (90.8, 38.8)
- added MH2: Mount-M2, MountingHole:MountingHole_2.2mm_M2_Pad, F.Cu at (71.0, 38.8)
- added MH2: Mount-M2, MountingHole:MountingHole_2.2mm_M2_Pad, F.Cu at (51.0, 38.8)
- added MH2: Mount-M2, MountingHole:MountingHole_2.2mm_M2_Pad, F.Cu at (50.8, 94.3)
- added MH2: Mount-M2, MountingHole:MountingHole_2.2mm_M2_Pad, F.Cu at (31.0, 38.8)
- added MH2: Mount-M2, MountingHole:MountingHole_2.2mm_M2_Pad, F.Cu at (111.0, 20.3)
- added MH2: Mount-M2, MountingHole:MountingHole_2.2mm_M2_Pad, F.Cu at (91.0, 20.3)
- added MH2: Mount-M2, MountingHole:MountingHole_2.2mm_M2_Pad, F.Cu at (71.0, 20.3)
- added MH2: Mount-M2, MountingHole:MountingHole_2.2mm_M2_Pad, F.Cu at (51.0, 20.3)
- added MH2: Mount-M2, MountingHole:MountingHole_2.2mm_M2_Pad, F.Cu at (31.0, 20.3)
- added MH2: Mount-M2, MountingHole:MountingHole_2.2mm_M2_Pad, F.Cu at (71.0, 94.3)
- added MH2: Mount-M2, MountingHole:MountingHole_2.2mm_M2_Pad, F.Cu at (91.0, 94.3)
- added MH2: Mount-M2, MountingHole:MountingHole_2.2mm_M2_Pad, F.Cu at (111.0, 94.3)
- added MH2: Mount-M2, MountingHole:MountingHole_2.2mm_M2_Pad, F.Cu at (111.0, 75.8)
- added MH2: Mount-M2, MountingHole:MountingHole_2.2mm_M2_Pad, F.Cu at (91.0, 75.8)
- added MH2: Mount-M2, MountingHole:MountingHole_2.2mm_M2_Pad, F.Cu at (71.0, 75.8)
- added MH2: Mount-M2, MountingHole:MountingHole_2.2mm_M2_Pad, F.Cu at (51.0, 75.8)
- added MH3: Mount-M2, MountingHole:MountingHole_2.2mm_M2_Pad_TopOnly, F.Cu at (17.0, 106.8)
- added MH3: Mount-M2, MountingHole:MountingHole_2.2mm_M2_Pad_TopOnly, F.Cu at (17.0, 88.3)
- added MH3: Mount-M2, MountingHole:MountingHole_2.2mm_M2_Pad_TopOnly, F.Cu at (17.0, 69.8)
- added MH3: Mount-M2, MountingHole:MountingHole_2.2mm_M2_Pad_TopOnly, F.Cu at (37.0, 69.8)
- added MH3: Mount-M2, MountingHole:MountingHole_2.2mm_M2_Pad_TopOnly, F.Cu at (57.0, 69.8)
- added MH3: Mount-M2, MountingHole:MountingHole_2.2mm_M2_Pad_TopOnly, F.Cu at (77.0, 69.8)
- added MH3: Mount-M2, MountingHole:MountingHole_2.2mm_M2_Pad_TopOnly, F.Cu at (97.0, 69.8)
- added MH3: Mount-M2, MountingHole:MountingHole_2.2mm_M2_Pad_TopOnly, F.Cu at (97.0, 51.3)
- added MH3: Mount-M2, MountingHole:MountingHole_2.2mm_M2_Pad_TopOnly, F.Cu at (76.8, 51.3)
- added MH3: Mount-M2, MountingHole:MountingHole_2.2mm_M2_Pad_TopOnly, F.Cu at (57.0, 51.3)
- added MH3: Mount-M2, MountingHole:MountingHole_2.2mm_M2_Pad_TopOnly, F.Cu at (37.0, 51.3)
- added MH3: Mount-M2, MountingHole:MountingHole_2.2mm_M2_Pad_TopOnly, F.Cu at (36.8, 106.8)
- added MH3: Mount-M2, MountingHole:MountingHole_2.2mm_M2_Pad_TopOnly, F.Cu at (17.0, 51.3)
- added MH3: Mount-M2, MountingHole:MountingHole_2.2mm_M2_Pad_TopOnly, F.Cu at (97.0, 32.8)
- added MH3: Mount-M2, MountingHole:MountingHole_2.2mm_M2_Pad_TopOnly, F.Cu at (77.0, 32.8)
- added MH3: Mount-M2, MountingHole:MountingHole_2.2mm_M2_Pad_TopOnly, F.Cu at (57.0, 32.8)
- added MH3: Mount-M2, MountingHole:MountingHole_2.2mm_M2_Pad_TopOnly, F.Cu at (37.0, 32.8)
- added MH3: Mount-M2, MountingHole:MountingHole_2.2mm_M2_Pad_TopOnly, F.Cu at (17.0, 32.8)
- added MH3: Mount-M2, MountingHole:MountingHole_2.2mm_M2_Pad_TopOnly, F.Cu at (57.0, 106.8)
- added MH3: Mount-M2, MountingHole:MountingHole_2.2mm_M2_Pad_TopOnly, F.Cu at (77.0, 106.8)
- added MH3: Mount-M2, MountingHole:MountingHole_2.2mm_M2_Pad_TopOnly, F.Cu at (97.0, 106.8)
- added MH3: Mount-M2, MountingHole:MountingHole_2.2mm_M2_Pad_TopOnly, F.Cu at (97.0, 88.3)
- added MH3: Mount-M2, MountingHole:MountingHole_2.2mm_M2_Pad_TopOnly, F.Cu at (77.0, 88.3)
- added MH3: Mount-M2, MountingHole:MountingHole_2.2mm_M2_Pad_TopOnly, F.Cu at (57.0, 88.3)
- added MH3: Mount-M2, MountingHole:MountingHole_2.2mm_M2_Pad_TopOnly, F.Cu at (37.0, 88.3)
- added MH4: Mount-M2, MountingHole:MountingHole_2.2mm_M2_Pad_TopOnly, F.Cu at (31.0, 106.8)
- added MH4: Mount-M2, MountingHole:MountingHole_2.2mm_M2_Pad_TopOnly, F.Cu at (31.0, 88.3)
- added MH4: Mount-M2, MountingHole:MountingHole_2.2mm_M2_Pad_TopOnly, F.Cu at (31.0, 69.8)
- added MH4: Mount-M2, MountingHole:MountingHole_2.2mm_M2_Pad_TopOnly, F.Cu at (51.0, 69.8)
- added MH4: Mount-M2, MountingHole:MountingHole_2.2mm_M2_Pad_TopOnly, F.Cu at (71.0, 69.8)
- added MH4: Mount-M2, MountingHole:MountingHole_2.2mm_M2_Pad_TopOnly, F.Cu at (91.0, 69.8)
- added MH4: Mount-M2, MountingHole:MountingHole_2.2mm_M2_Pad_TopOnly, F.Cu at (111.0, 69.8)
- added MH4: Mount-M2, MountingHole:MountingHole_2.2mm_M2_Pad_TopOnly, F.Cu at (111.0, 51.3)
- added MH4: Mount-M2, MountingHole:MountingHole_2.2mm_M2_Pad_TopOnly, F.Cu at (90.8, 51.3)
- added MH4: Mount-M2, MountingHole:MountingHole_2.2mm_M2_Pad_TopOnly, F.Cu at (71.0, 51.3)
- added MH4: Mount-M2, MountingHole:MountingHole_2.2mm_M2_Pad_TopOnly, F.Cu at (51.0, 51.3)
- added MH4: Mount-M2, MountingHole:MountingHole_2.2mm_M2_Pad_TopOnly, F.Cu at (50.8, 106.8)
- added MH4: Mount-M2, MountingHole:MountingHole_2.2mm_M2_Pad_TopOnly, F.Cu at (31.0, 51.3)
- added MH4: Mount-M2, MountingHole:MountingHole_2.2mm_M2_Pad_TopOnly, F.Cu at (111.0, 32.8)
- added MH4: Mount-M2, MountingHole:MountingHole_2.2mm_M2_Pad_TopOnly, F.Cu at (91.0, 32.8)
- added MH4: Mount-M2, MountingHole:MountingHole_2.2mm_M2_Pad_TopOnly, F.Cu at (71.0, 32.8)
- added MH4: Mount-M2, MountingHole:MountingHole_2.2mm_M2_Pad_TopOnly, F.Cu at (51.0, 32.8)
- added MH4: Mount-M2, MountingHole:MountingHole_2.2mm_M2_Pad_TopOnly, F.Cu at (31.0, 32.8)
- added MH4: Mount-M2, MountingHole:MountingHole_2.2mm_M2_Pad_TopOnly, F.Cu at (71.0, 106.8)
- added MH4: Mount-M2, MountingHole:MountingHole_2.2mm_M2_Pad_TopOnly, F.Cu at (91.0, 106.8)
- added MH4: Mount-M2, MountingHole:MountingHole_2.2mm_M2_Pad_TopOnly, F.Cu at (111.0, 106.8)
- added MH4: Mount-M2, MountingHole:MountingHole_2.2mm_M2_Pad_TopOnly, F.Cu at (111.0, 88.3)
- added MH4: Mount-M2, MountingHole:MountingHole_2.2mm_M2_Pad_TopOnly, F.Cu at (91.0, 88.3)
- added MH4: Mount-M2, MountingHole:MountingHole_2.2mm_M2_Pad_TopOnly, F.Cu at (71.0, 88.3)
- added MH4: Mount-M2, MountingHole:MountingHole_2.2mm_M2_Pad_TopOnly, F.Cu at (51.0, 88.3)
- added R1: 5.1k, Resistor_SMD:R_0603_1608Metric_Pad0.98x0.95mm_HandSolder, F.Cu at (16.1, 98.2)
- added R1: 5.1k, Resistor_SMD:R_0603_1608Metric_Pad0.98x0.95mm_HandSolder, F.Cu at (16.1, 79.7)
- added R1: 5.1k, Resistor_SMD:R_0603_1608Metric_Pad0.98x0.95mm_HandSolder, F.Cu at (16.1, 61.2)
- added R1: 5.1k, Resistor_SMD:R_0603_1608Metric_Pad0.98x0.95mm_HandSolder, F.Cu at (36.1, 61.2)
- added R1: 5.1k, Resistor_SMD:R_0603_1608Metric_Pad0.98x0.95mm_HandSolder, F.Cu at (56.1, 61.2)
- added R1: 5.1k, Resistor_SMD:R_0603_1608Metric_Pad0.98x0.95mm_HandSolder, F.Cu at (76.1, 61.2)
- added R1: 5.1k, Resistor_SMD:R_0603_1608Metric_Pad0.98x0.95mm_HandSolder, F.Cu at (96.1, 61.2)
- added R1: 5.1k, Resistor_SMD:R_0603_1608Metric_Pad0.98x0.95mm_HandSolder, F.Cu at (96.1, 42.7)
- added R1: 5.1k, Resistor_SMD:R_0603_1608Metric_Pad0.98x0.95mm_HandSolder, F.Cu at (75.9, 42.7)
- added R1: 5.1k, Resistor_SMD:R_0603_1608Metric_Pad0.98x0.95mm_HandSolder, F.Cu at (56.1, 42.7)
- added R1: 5.1k, Resistor_SMD:R_0603_1608Metric_Pad0.98x0.95mm_HandSolder, F.Cu at (36.1, 42.7)
- added R1: 5.1k, Resistor_SMD:R_0603_1608Metric_Pad0.98x0.95mm_HandSolder, F.Cu at (35.9, 98.2)
- added R1: 5.1k, Resistor_SMD:R_0603_1608Metric_Pad0.98x0.95mm_HandSolder, F.Cu at (16.1, 42.7)
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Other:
- board size 94 x 95.5 mm -> 98 x 96 mm
